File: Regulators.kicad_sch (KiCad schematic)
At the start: 38 parts, among them J3 5V_SUPPLY, J4 5V_AUXOUT, J5 24V Power Inlet, U2 TPS5430DDAR, U3 TPS5430DDAR, U4 TPS5430DDAR

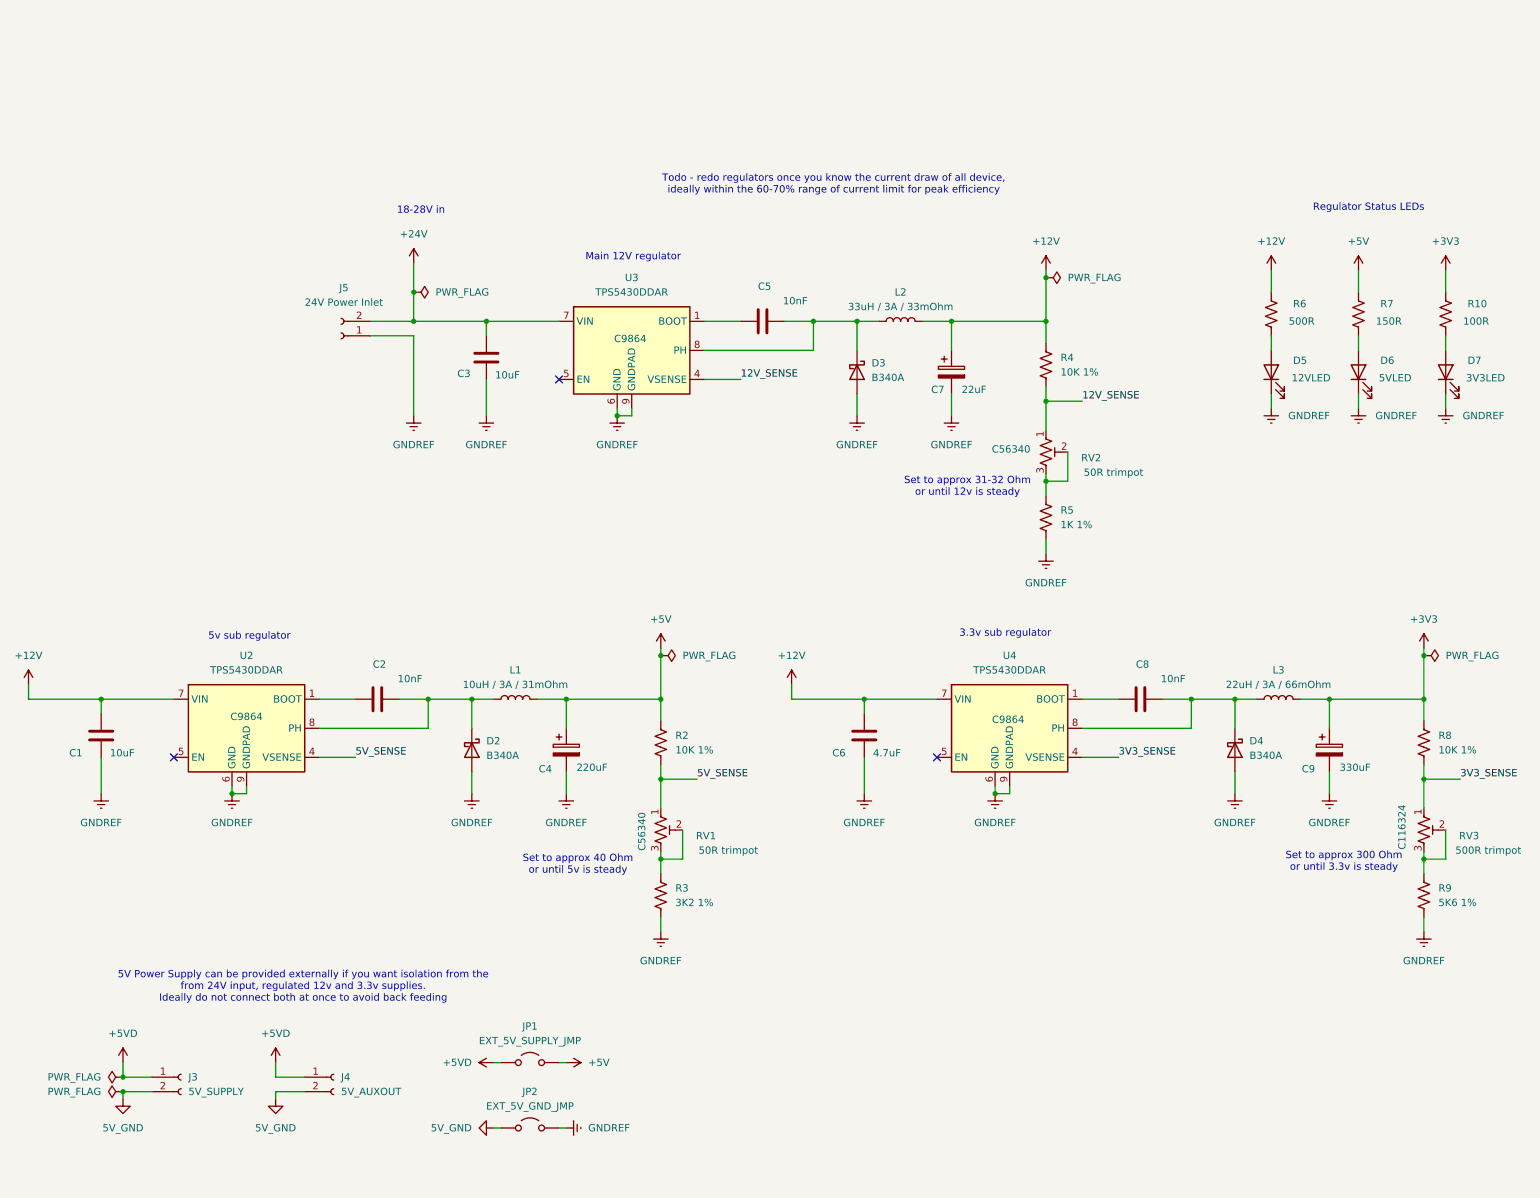
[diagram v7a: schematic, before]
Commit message: restructured power supplies to enable Spindle DAC to be isolated. We now have the option of supplying two 24V inputs, one to power the nucleo and everything logic side and the other to power peripherals. Some testing will be required.
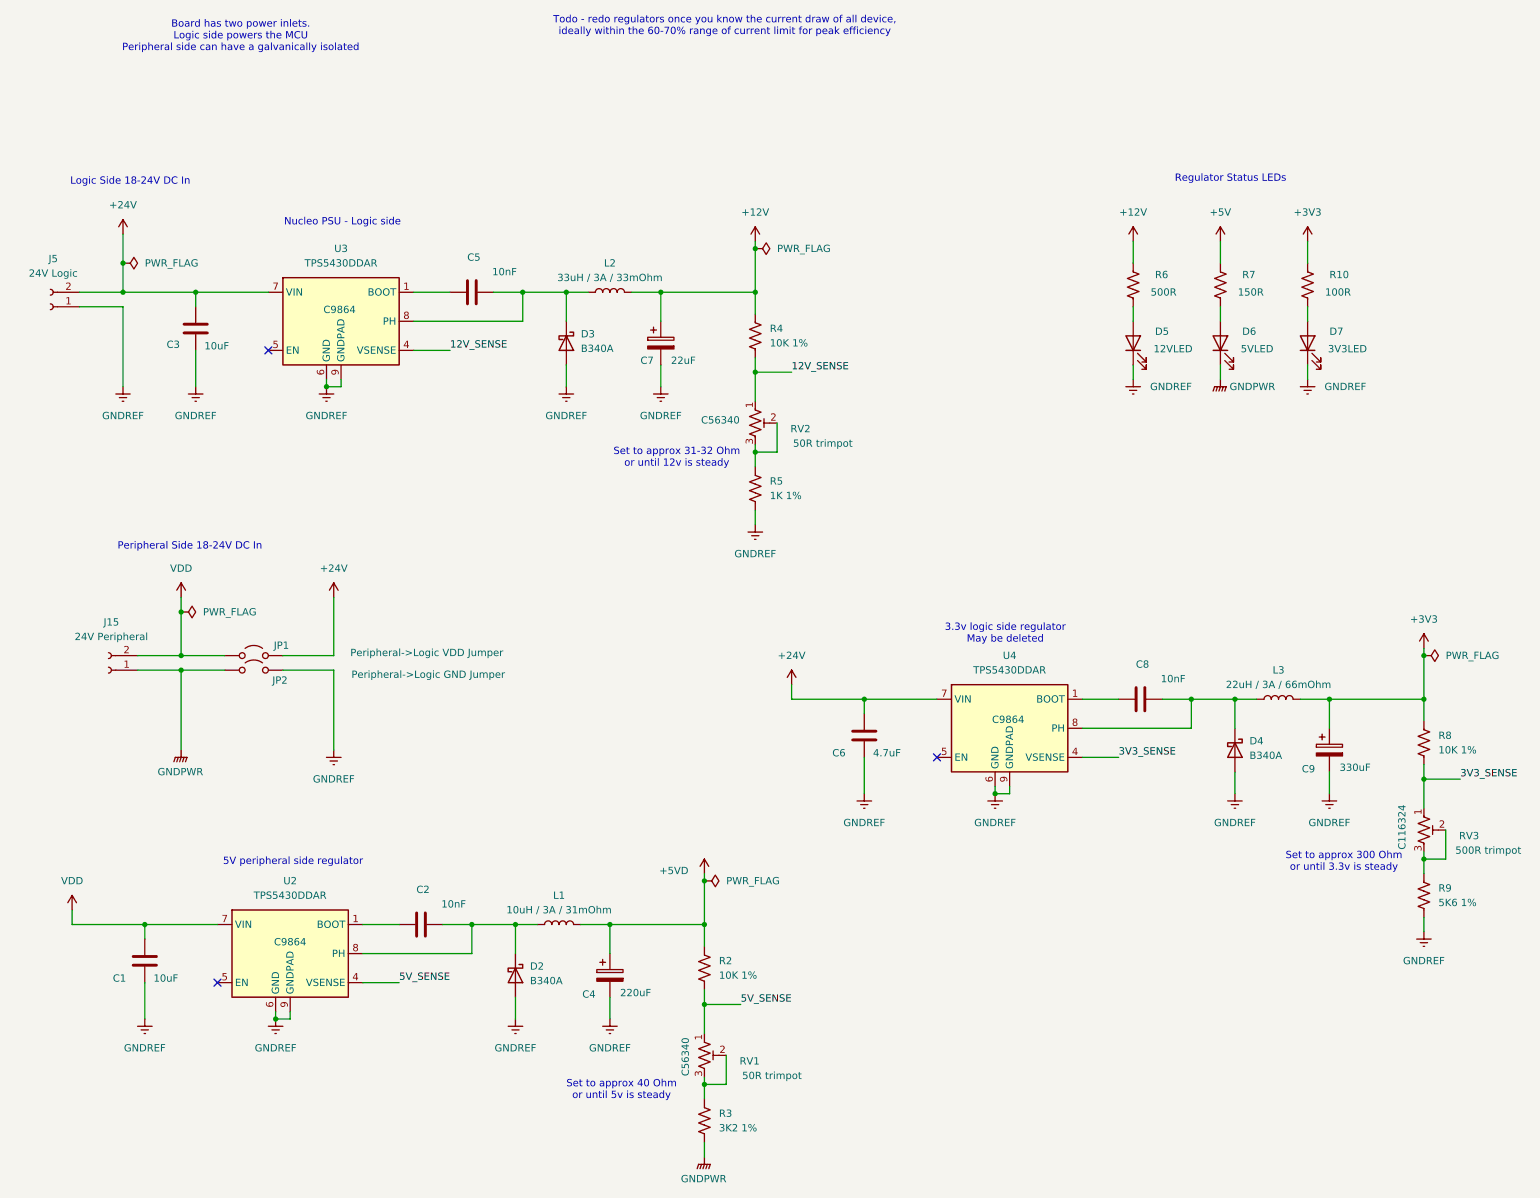
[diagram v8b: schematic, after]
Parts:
- removed J3: 5V_SUPPLY, OSTVTerminalBlocks:Conn01x02, symbol Connector:Conn_01x02_Socket
- removed J4: 5V_AUXOUT, OSTVTerminalBlocks:Conn01x02, symbol Connector:Conn_01x02_Socket
- added J15: 24V Peripheral, OSTVTerminalBlocks:Conn01x02, symbol Connector:Conn_01x02_Socket
- J5: value 24V Power Inlet -> 24V Logic
- JP1: value EXT_5V_SUPPLY_JMP -> Peripheral->Logic VDD Jumper; footprint Jumper:SolderJumper-2_P1.3mm_Open_TrianglePad1.0x1.5mm -> (none); now in the parts list
- JP2: value EXT_5V_GND_JMP -> Peripheral->Logic GND Jumper; footprint Jumper:SolderJumper-2_P1.3mm_Open_TrianglePad1.0x1.5mm -> (none); now in the parts list
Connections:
- net +12V: no longer C1.1, C6.1, U2.7 (VIN), U4.7 (VIN)
- net +24V: now also C6.1, JP1.2 (B), U4.7 (VIN)
- net +5V: no longer C4.1, JP1.2 (B), L1.2, R2.1
- net +5VD: now also C4.1, L1.2, R2.1; no longer JP1.1 (A)
- net GNDREF: no longer D6.1 (K), R3.2
- net 5V_GND renamed GNDPWR
- net GNDPWR: now also D6.1 (K), R3.2, J15.1 (Pin_1)
- new net VDD: C1.1, J15.2 (Pin_2), JP1.1 (A), U2.7 (VIN)
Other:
- note added: "3.3v logic side regulator May be deleted"
- note added: "5V peripheral side regulator"
- note added: "Board has two power inlets. Logic side powers the MCU Peripheral side can have a galvanically isolated"
- note added: "Logic Side 18-24V DC In"
- note added: "Nucleo PSU - Logic side"
- note added: "Peripheral Side 18-24V DC In"
- note removed: "18-28V in"
- note removed: "3.3v sub regulator"
- note removed: "5V Power Supply can be provided externally if you want isolation from the from 24V input, regulated 12v and 3.3v supplies. Ideally do not connect both at once to avoid back feeding"
- note removed: "5v sub regulator"
- note removed: "Main 12V regulator"
- moved on the sheet: C1, C2, C3, C4, C5, C7, D2, D3, D5, D6, D7, J5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
